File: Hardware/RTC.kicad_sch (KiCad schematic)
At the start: 15 parts, among them IC1 RTC_DS3231M, U8 PCF8563TS, Y2 32.768kHz

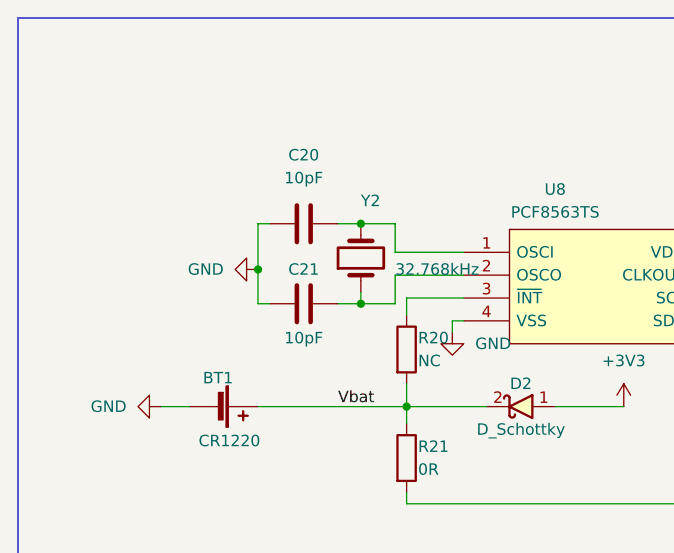
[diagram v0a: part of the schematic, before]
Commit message: Change footprint of MCP41010 and 32.768 crystal
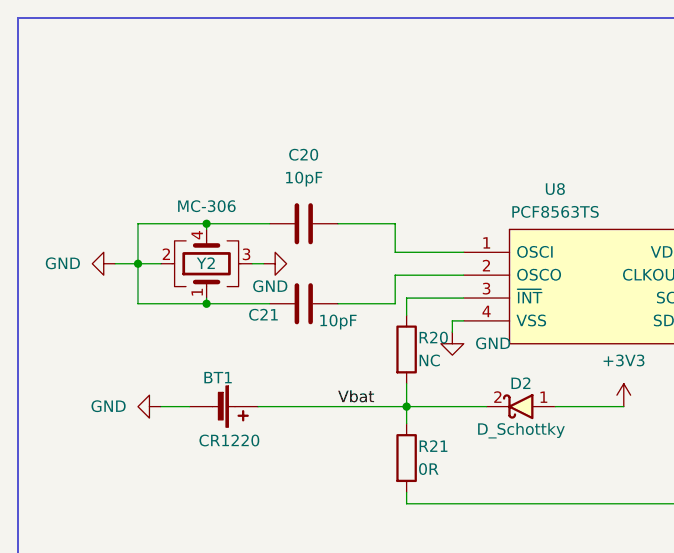
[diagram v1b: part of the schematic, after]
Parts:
- removed Y2: 32.768kHz, Crystal:Crystal_SMD_SeikoEpson_MC306-4Pin_8.0x3.2mm, symbol Device:Crystal
- added Y2: MC-306, Crystal:Crystal_SMD_SeikoEpson_MC306-4Pin_8.0x3.2mm, symbol Device:Crystal_GND23
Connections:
- net GND: now also Y2.1, Y2.2, Y2.3, Y2.4
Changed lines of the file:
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@@
 (kicad_sch (version 20211123) (generator eeschema)
   (paper "A4")
-  (junction (at 63.5 52.07) (diameter 0) (color 0 0 0 0)
-  )
-  (junction (at 74.93 55.88) (diameter 0) (color 0 0 0 0)
+  (junction (at 50.165 51.435) (diameter 0) (color 0 0 0 0)
   )
   (junction (at 118.11 50.165) (diameter 0) (color 0 0 0 0)
   )
-  (junction (at 74.93 46.99) (diameter 0) (color 0 0 0 0)
+  (junction (at 57.785 46.99) (diameter 0) (color 0 0 0 0)
   )
   (junction (at 80.01 67.31) (diameter 0) (color 0 0 0 0)
@@
   )
   (junction (at 201.93 46.99) (diameter 0) (color 0 0 0 0)
+  )
+  (junction (at 57.785 55.88) (diameter 0) (color 0 0 0 0)
   )
   (junction (at 215.9 52.07) (diameter 0) (color 0 0 0 0)
@@
     (stroke (width 0) (type default) (color 0 0 0 0))
   )
+  (wire (pts (xy 47.625 51.435) (xy 50.165 51.435))
+    (stroke (width 0) (type default) (color 0 0 0 0))
+  )
   (wire (pts (xy 218.44 43.18) (xy 218.44 55.88))
     (stroke (width 0) (type default) (color 0 0 0 0))
@@
     (stroke (width 0) (type default) (color 0 0 0 0))
   )
+  (wire (pts (xy 50.165 51.435) (xy 52.705 51.435))
+    (stroke (width 0) (type default) (color 0 0 0 0))
+  )
   (wire (pts (xy 218.44 43.18) (xy 231.14 43.18))
     (stroke (width 0) (type default) (color 0 0 0 0))
   )
+  (wire (pts (xy 57.785 55.245) (xy 57.785 55.88))
+    (stroke (width 0) (type default) (color 0 0 0 0))
+  )
   (wire (pts (xy 205.74 43.18) (xy 201.93 43.18))
     (stroke (width 0) (type default) (color 0 0 0 0))
@@
     (stroke (width 0) (type default) (color 0 0 0 0))
   )
+  (wire (pts (xy 50.165 46.99) (xy 57.785 46.99))
+    (stroke (width 0) (type default) (color 0 0 0 0))
+  )
   (wire (pts (xy 80.01 67.31) (xy 88.9 67.31))
     (stroke (width 0) (type default) (color 0 0 0 0))
   )
-  (wire (pts (xy 74.93 54.61) (xy 74.93 55.88))
-    (stroke (width 0) (type default) (color 0 0 0 0))
-  )
   (wire (pts (xy 78.74 52.705) (xy 86.36 52.705))
     (stroke (width 0) (type default) (color 0 0 0 0))
@@
     (stroke (width 0) (type default) (color 0 0 0 0))
   )
-  (wire (pts (xy 63.5 52.07) (xy 63.5 55.88))
-    (stroke (width 0) (type default) (color 0 0 0 0))
-  )
   (wire (pts (xy 199.39 46.99) (xy 201.93 46.99))
     (stroke (width 0) (type default) (color 0 0 0 0))
@@
     (stroke (width 0) (type default) (color 0 0 0 0))
   )
-  (wire (pts (xy 64.77 55.88) (xy 63.5 55.88))
-    (stroke (width 0) (type default) (color 0 0 0 0))
-  )
   (wire (pts (xy 80.01 69.215) (xy 80.01 67.31))
     (stroke (width 0) (type default) (color 0 0 0 0))
@@
     (stroke (width 0) (type default) (color 0 0 0 0))
   )
-  (wire (pts (xy 63.5 46.99) (xy 64.77 46.99))
-    (stroke (width 0) (type default) (color 0 0 0 0))
-  )
   (wire (pts (xy 118.11 33.655) (xy 118.11 36.83))
     (stroke (width 0) (type default) (color 0 0 0 0))
@@
     (stroke (width 0) (type default) (color 0 0 0 0))
   )
+  (wire (pts (xy 57.785 55.88) (xy 64.77 55.88))
+    (stroke (width 0) (type default) (color 0 0 0 0))
+  )
   (polyline (pts (xy 170.18 104.14) (xy 264.16 104.14))
     (stroke (width 0) (type default) (color 0 0 0 0))
@@
     (stroke (width 0) (type default) (color 0 0 0 0))
   )
-  (wire (pts (xy 63.5 46.99) (xy 63.5 52.07))
+  (wire (pts (xy 50.165 46.99) (xy 50.165 51.435))
     (stroke (width 0) (type default) (color 0 0 0 0))
   )
@@
     (stroke (width 0) (type default) (color 0 0 0 0))
   )
+  (wire (pts (xy 57.785 46.99) (xy 57.785 47.625))
+    (stroke (width 0) (type default) (color 0 0 0 0))
+  )
   (polyline (pts (xy 170.18 25.4) (xy 170.18 104.14))
     (stroke (width 0) (type default) (color 0 0 0 0))
@@
     (stroke (width 0) (type default) (color 0 0 0 0))
   )
-  (wire (pts (xy 72.39 46.99) (xy 74.93 46.99))
-    (stroke (width 0) (type default) (color 0 0 0 0))
-  )
   (wire (pts (xy 78.74 52.705) (xy 78.74 55.88))
     (stroke (width 0) (type default) (color 0 0 0 0))
   )
+  (wire (pts (xy 62.865 51.435) (xy 64.135 51.435))
+    (stroke (width 0) (type default) (color 0 0 0 0))
+  )
   (wire (pts (xy 215.9 43.18) (xy 215.9 52.07))
     (stroke (width 0) (type default) (color 0 0 0 0))
@@
     (stroke (width 0) (type default) (color 0 0 0 0))
   )
+  (wire (pts (xy 50.165 51.435) (xy 50.165 55.88))
+    (stroke (width 0) (type default) (color 0 0 0 0))
+  )
   (wire (pts (xy 86.36 50.165) (xy 78.74 50.165))
     (stroke (width 0) (type default) (color 0 0 0 0))
@@
     (stroke (width 0) (type default) (color 0 0 0 0))
   )
-  (wire (pts (xy 72.39 55.88) (xy 74.93 55.88))
+  (wire (pts (xy 72.39 55.88) (xy 78.74 55.88))
     (stroke (width 0) (type default) (color 0 0 0 0))
   )
@@
     (stroke (width 0) (type default) (color 0 0 0 0))
   )
+  (wire (pts (xy 57.785 46.99) (xy 64.77 46.99))
+    (stroke (width 0) (type default) (color 0 0 0 0))
+  )
   (wire (pts (xy 80.01 78.105) (xy 118.11 78.105))
     (stroke (width 0) (type default) (color 0 0 0 0))
   )
-  (wire (pts (xy 74.93 55.88) (xy 78.74 55.88))
-    (stroke (width 0) (type default) (color 0 0 0 0))
-  )
   (wire (pts (xy 243.84 43.18) (xy 243.84 41.91))
     (stroke (width 0) (type default) (color 0 0 0 0))
   )
-  (wire (pts (xy 74.93 46.99) (xy 78.74 46.99))
+  (wire (pts (xy 72.39 46.99) (xy 78.74 46.99))
     (stroke (width 0) (type default) (color 0 0 0 0))
   )
@@
   )
   (polyline (pts (xy 264.16 24.13) (xy 170.18 24.13))
+    (stroke (width 0) (type default) (color 0 0 0 0))
+  )
+  (wire (pts (xy 50.165 55.88) (xy 57.785 55.88))
     (stroke (width 0) (type default) (color 0 0 0 0))
   )
@@
     )
     (property "Datasheet" "" (id 3) (at 231.14 45.72 0)
-      (effects (font (size 1.27 1.27)) hide)
-    )
-    (pin "1")
-    (pin "2")
-  )
-  (symbol (lib_id "Device:Crystal") (at 74.93 50.8 90) (unit 1)
-    (in_bom yes) (on_board yes)
-    (property "Reference" "Y2" (id 0) (at 74.93 44.45 90)
-      (effects (font (size 1.27 1.27)) (justify right))
-    )
-    (property "Value" "32.768kHz" (id 1) (at 78.74 52.07 90)
-      (effects (font (size 1.27 1.27)) (justify right))
-    )
-    (property "Footprint" "Crystal:Crystal_SMD_SeikoEpson_MC306-4Pin_8.0x3.2mm" (id 2) (at 74.93 50.8 0)
-      (effects (font (size 1.27 1.27)) hide)
-    )
-    (property "Datasheet" "~" (id 3) (at 74.93 50.8 0)
       (effects (font (size 1.27 1.27)) hide)
     )
@@
   (symbol (lib_id "Device:C") (at 68.58 55.88 90) (unit 1)
     (in_bom yes) (on_board yes)
-    (property "Reference" "C21" (id 0) (at 68.58 52.07 90))
-    (property "Value" "10pF" (id 1) (at 68.58 59.69 90))
+    (property "Reference" "C21" (id 0) (at 64.135 57.15 90))
+    (property "Value" "10pF" (id 1) (at 72.39 57.785 90))
     (property "Footprint" "IVS_FOOTPRINTS:C0603" (id 2) (at 72.39 54.9148 0)
       (effects (font (size 1.27 1.27)) hide)
@@
     (pin "2")
   )
-  (symbol (lib_id "power:GND") (at 63.5 52.07 270) (unit 1)
-    (in_bom yes) (on_board yes) (fields_autoplaced)
-    (property "Reference" "#PWR052" (id 0) (at 57.15 52.07 0)
-      (effects (font (size 1.27 1.27)) hide)
-    )
-    (property "Value" "GND" (id 1) (at 59.69 52.0699 90)
+  (symbol (lib_id "power:GND") (at 47.625 51.435 270) (unit 1)
+    (in_bom yes) (on_board yes) (fields_autoplaced)
+    (property "Reference" "#PWR052" (id 0) (at 41.275 51.435 0)
+      (effects (font (size 1.27 1.27)) hide)
+    )
+    (property "Value" "GND" (id 1) (at 43.815 51.4349 90)
       (effects (font (size 1.27 1.27)) (justify right))
     )
-    (property "Footprint" "" (id 2) (at 63.5 52.07 0)
-      (effects (font (size 1.27 1.27)) hide)
-    )
-    (property "Datasheet" "" (id 3) (at 63.5 52.07 0)
+    (property "Footprint" "" (id 2) (at 47.625 51.435 0)
+      (effects (font (size 1.27 1.27)) hide)
+    )
+    (property "Datasheet" "" (id 3) (at 47.625 51.435 0)
       (effects (font (size 1.27 1.27)) hide)
     )
@@
     (pin "1")
   )
+  (symbol (lib_id "power:GND") (at 64.135 51.435 90) (unit 1)
+    (in_bom yes) (on_board yes)
+    (property "Reference" "#PWR0182" (id 0) (at 70.485 51.435 0)
+      (effects (font (size 1.27 1.27)) hide)
+    )
+    (property "Value" "GND" (id 1) (at 62.865 53.975 90)
+      (effects (font (size 1.27 1.27)) (justify right))
+    )
+    (property "Footprint" "" (id 2) (at 64.135 51.435 0)
+      (effects (font (size 1.27 1.27)) hide)
+    )
+    (property "Datasheet" "" (id 3) (at 64.135 51.435 0)
+      (effects (font (size 1.27 1.27)) hide)
+    )
+    (pin "1")
+  )
   (symbol (lib_id "power:+3V3") (at 243.84 41.91 0) (unit 1)
     (in_bom yes) (on_board yes) (fields_autoplaced)
@@
     (pin "2")
   )
+  (symbol (lib_id "Device:Crystal_GND23") (at 57.785 51.435 90) (unit 1)
+    (in_bom yes) (on_board yes)
+    (property "Reference" "Y2" (id 0) (at 57.785 51.435 90))
+    (property "Value" "MC-306" (id 1) (at 57.785 45.085 90))
+    (property "Footprint" "Crystal:Crystal_SMD_SeikoEpson_MC306-4Pin_8.0x3.2mm" (id 2) (at 57.785 51.435 0)
+      (effects (font (size 1.27 1.27)) hide)
+    )
+    (property "Datasheet" "~" (id 3) (at 57.785 51.435 0)
+      (effects (font (size 1.27 1.27)) hide)
+    )
+    (pin "1")
+    (pin "2")
+    (pin "3")
+    (pin "4")
+  )
   (symbol (lib_id "power:GND") (at 52.705 67.31 270) (unit 1)

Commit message: add shematics MVA
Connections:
- net GND: now also C20.2, C21.2; no longer C20.1, C21.1, Y2.1, Y2.4
- net at U8.2 (OSCO): now also C21.1, Y2.1; no longer C21.2
- net at U8.1 (OSCI): now also C20.1, Y2.4; no longer C20.2
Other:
- moved on the sheet: C20, C21
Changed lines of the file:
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@@
 (kicad_sch (version 20230121) (generator eeschema)
   (paper "A4")
-  (junction (at 50.165 51.435) (diameter 0) (color 0 0 0 0)
+  (junction (at 70.485 52.07) (diameter 0) (color 0 0 0 0)
   )
   (junction (at 118.11 50.165) (diameter 0) (color 0 0 0 0)
@@
     (stroke (width 0) (type default))
   )
-  (wire (pts (xy 47.625 51.435) (xy 50.165 51.435))
+  (wire (pts (xy 69.215 52.07) (xy 70.485 52.07))
     (stroke (width 0) (type default))
   )
@@
     (stroke (width 0) (type default))
   )
-  (wire (pts (xy 50.165 51.435) (xy 52.705 51.435))
-    (stroke (width 0) (type default))
-  )
   (wire (pts (xy 218.44 43.18) (xy 231.14 43.18))
     (stroke (width 0) (type default))
@@
     (stroke (width 0) (type default))
   )
+  (wire (pts (xy 70.485 52.07) (xy 71.755 52.07))
+    (stroke (width 0) (type default))
+  )
   (polyline (pts (xy 170.18 24.13) (xy 170.18 25.4))
     (stroke (width 0) (type default))
@@
     (stroke (width 0) (type default))
   )
-  (wire (pts (xy 50.165 46.99) (xy 57.785 46.99))
-    (stroke (width 0) (type default))
-  )
   (wire (pts (xy 80.01 67.31) (xy 88.9 67.31))
     (stroke (width 0) (type default))
@@
     (stroke (width 0) (type default))
   )
+  (wire (pts (xy 68.58 55.88) (xy 70.485 55.88))
+    (stroke (width 0) (type default))
+  )
   (polyline (pts (xy 36.83 24.13) (xy 36.83 104.14))
     (stroke (width 0) (type default))
@@
     (stroke (width 0) (type default))
   )
+  (wire (pts (xy 69.215 51.435) (xy 62.865 51.435))
+    (stroke (width 0) (type default))
+  )
   (wire (pts (xy 199.39 46.99) (xy 201.93 46.99))
     (stroke (width 0) (type default))
@@
     (stroke (width 0) (type default))
   )
+  (wire (pts (xy 78.74 59.69) (xy 57.785 59.69))
+    (stroke (width 0) (type default))
+  )
   (wire (pts (xy 118.11 33.655) (xy 118.11 36.83))
     (stroke (width 0) (type default))
   )
+  (wire (pts (xy 70.485 46.99) (xy 70.485 52.07))
+    (stroke (width 0) (type default))
+  )
   (bus (pts (xy 134.62 64.77) (xy 137.16 64.77))
     (stroke (width 0) (type default))
@@
     (stroke (width 0) (type default))
   )
-  (wire (pts (xy 57.785 55.88) (xy 64.77 55.88))
+  (wire (pts (xy 57.785 55.88) (xy 60.96 55.88))
     (stroke (width 0) (type default))
   )
@@
     (stroke (width 0) (type default))
   )
-  (wire (pts (xy 78.74 46.99) (xy 78.74 50.165))
-    (stroke (width 0) (type default))
-  )
-  (wire (pts (xy 50.165 46.99) (xy 50.165 51.435))
+  (wire (pts (xy 78.74 43.18) (xy 78.74 50.165))
+    (stroke (width 0) (type default))
+  )
+  (wire (pts (xy 68.58 46.99) (xy 70.485 46.99))
     (stroke (width 0) (type default))
   )
@@
     (stroke (width 0) (type default))
   )
-  (wire (pts (xy 78.74 52.705) (xy 78.74 55.88))
-    (stroke (width 0) (type default))
-  )
-  (wire (pts (xy 62.865 51.435) (xy 64.135 51.435))
+  (wire (pts (xy 78.74 52.705) (xy 78.74 59.69))
+    (stroke (width 0) (type default))
+  )
+  (wire (pts (xy 57.785 46.99) (xy 60.96 46.99))
     (stroke (width 0) (type default))
   )
@@
     (stroke (width 0) (type default))
   )
-  (wire (pts (xy 50.165 51.435) (xy 50.165 55.88))
+  (wire (pts (xy 78.74 43.18) (xy 57.785 43.18))
     (stroke (width 0) (type default))
   )
@@
     (stroke (width 0) (type default))
   )
+  (wire (pts (xy 70.485 52.07) (xy 70.485 55.88))
+    (stroke (width 0) (type default))
+  )
   (wire (pts (xy 215.9 41.91) (xy 215.9 43.18))
     (stroke (width 0) (type default))
@@
     (stroke (width 0) (type default))
   )
+  (wire (pts (xy 69.215 52.07) (xy 69.215 51.435))
+    (stroke (width 0) (type default))
+  )
   (wire (pts (xy 201.93 43.18) (xy 201.93 46.99))
     (stroke (width 0) (type default))
   )
-  (wire (pts (xy 72.39 55.88) (xy 78.74 55.88))
+  (wire (pts (xy 57.785 43.18) (xy 57.785 46.99))
     (stroke (width 0) (type default))
   )
@@
     (stroke (width 0) (type default))
   )
-  (wire (pts (xy 57.785 46.99) (xy 64.77 46.99))
+  (wire (pts (xy 57.785 59.69) (xy 57.785 55.88))
     (stroke (width 0) (type default))
   )
@@
     (stroke (width 0) (type default))
   )
-  (wire (pts (xy 72.39 46.99) (xy 78.74 46.99))
-    (stroke (width 0) (type default))
-  )
   (wire (pts (xy 85.09 59.055) (xy 85.09 57.785))
     (stroke (width 0) (type default))
   )
   (polyline (pts (xy 264.16 24.13) (xy 170.18 24.13))
-    (stroke (width 0) (type default))
-  )
-  (wire (pts (xy 50.165 55.88) (xy 57.785 55.88))
     (stroke (width 0) (type default))
   )
@@
     )
   )
-  (symbol (lib_id "Device:C") (at 68.58 55.88 90) (unit 1)
+  (symbol (lib_id "Device:C") (at 64.77 55.88 90) (unit 1)
     (in_bom yes) (on_board yes) (dnp no)
-    (property "Reference" "C21" (at 64.135 57.15 90)
-      (effects (font (size 1.27 1.27)))
-    )
-    (property "Value" "10pF" (at 72.39 57.785 90)
-      (effects (font (size 1.27 1.27)))
-    )
-    (property "Footprint" "IVS_FOOTPRINTS:C0603" (at 72.39 54.9148 0)
-      (effects (font (size 1.27 1.27)) hide)
-    )
-    (property "Datasheet" "~" (at 68.58 55.88 0)
+    (property "Reference" "C21" (at 60.325 57.15 90)
+      (effects (font (size 1.27 1.27)))
+    )
+    (property "Value" "10pF" (at 68.58 57.785 90)
+      (effects (font (size 1.27 1.27)))
+    )
+    (property "Footprint" "IVS_FOOTPRINTS:C0603" (at 68.58 54.9148 0)
+      (effects (font (size 1.27 1.27)) hide)
+    )
+    (property "Datasheet" "~" (at 64.77 55.88 0)
       (effects (font (size 1.27 1.27)) hide)
     )
@@
     )
   )
-  (symbol (lib_id "power:GND") (at 47.625 51.435 270) (unit 1)
-    (in_bom yes) (on_board yes) (dnp no) (fields_autoplaced)
-    (property "Reference" "#PWR052" (at 41.275 51.435 0)
-      (effects (font (size 1.27 1.27)) hide)
-    )
-    (property "Value" "GND" (at 43.815 51.4349 90)
+  (symbol (lib_id "power:GND") (at 52.705 51.435 270) (unit 1)
+    (in_bom yes) (on_board yes) (dnp no) (fields_autoplaced)
+    (property "Reference" "#PWR052" (at 46.355 51.435 0)
+      (effects (font (size 1.27 1.27)) hide)
+    )
+    (property "Value" "GND" (at 48.895 51.4349 90)
       (effects (font (size 1.27 1.27)) (justify right))
     )
-    (property "Footprint" "" (at 47.625 51.435 0)
-      (effects (font (size 1.27 1.27)) hide)
-    )
-    (property "Datasheet" "" (at 47.625 51.435 0)
+    (property "Footprint" "" (at 52.705 51.435 0)
+      (effects (font (size 1.27 1.27)) hide)
+    )
+    (property "Datasheet" "" (at 52.705 51.435 0)
       (effects (font (size 1.27 1.27)) hide)
     )
@@
     )
   )
-  (symbol (lib_id "power:GND") (at 64.135 51.435 90) (unit 1)
+  (symbol (lib_id "power:GND") (at 71.755 52.07 90) (unit 1)
     (in_bom yes) (on_board yes) (dnp no)
-    (property "Reference" "#PWR0182" (at 70.485 51.435 0)
-      (effects (font (size 1.27 1.27)) hide)
-    )
-    (property "Value" "GND" (at 62.865 53.975 90)
+    (property "Reference" "#PWR0182" (at 78.105 52.07 0)
+      (effects (font (size 1.27 1.27)) hide)
+    )
+    (property "Value" "GND" (at 70.485 54.61 90)
       (effects (font (size 1.27 1.27)) (justify right))
     )
-    (property "Footprint" "" (at 64.135 51.435 0)
-      (effects (font (size 1.27 1.27)) hide)
-    )
-    (property "Datasheet" "" (at 64.135 51.435 0)
+    (property "Footprint" "" (at 71.755 52.07 0)
+      (effects (font (size 1.27 1.27)) hide)
+    )
+    (property "Datasheet" "" (at 71.755 52.07 0)
       (effects (font (size 1.27 1.27)) hide)
     )
@@
     )
   )
-  (symbol (lib_id "Device:C") (at 68.58 46.99 90) (unit 1)
-    (in_bom yes) (on_board yes) (dnp no) (fields_autoplaced)
-    (property "Reference" "C20" (at 68.58 39.37 90)
-      (effects (font (size 1.27 1.27)))
-    )
-    (property "Value" "10pF" (at 68.58 41.91 90)
-      (effects (font (size 1.27 1.27)))
-    )
-    (property "Footprint" "IVS_FOOTPRINTS:C0603" (at 72.39 46.0248 0)
-      (effects (font (size 1.27 1.27)) hide)
-    )
-    (property "Datasheet" "~" (at 68.58 46.99 0)
-      (effects (font (size 1.27 1.27)) hide)
-    )
+  (symbol (lib_id "Device:C") (at 64.77 46.99 90) (unit 1)
+    (in_bom yes) (on_board yes) (dnp no) (fields_autoplaced)
+    (property "Reference" "C20" (at 64.77 39.37 90)
+      (effects (font (size 1.27 1.27)))
+    )
+    (property "Value" "10pF" (at 64.77 41.91 90)
+      (effects (font (size 1.27 1.27)))
+    )
+    (property "Footprint" "IVS_FOOTPRINTS:C0603" (at 68.58 46.0248 0)
+      (effects (font (size 1.27 1.27)) hide)
+    )
+    (property "Datasheet" "~" (at 64.77 46.99 0)
+      (effects (font (size 1.27 1.27)) hide)
+    )

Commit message: layout PCB part 1
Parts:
- removed D2, D3, D4: D_Schottky, IVS_FOOTPRINTS:D_SMA, symbol IVS_SYMBOL_DIR:D_Schottky
- added D1, D2: BAT54C, IVS_FOOTPRINTS:SOT23-3, symbol IVS_SYMBOLS:BAT54C
- added R42: 1k, IVS_FOOTPRINTS:R0603, symbol Device:R
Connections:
- net +3V3: now also D2.3, R42.1
- net Vbat: now also D1.2, D2.2
- net at IC1.14 (VBAT): now also D1.3
- new net: D1.1, R42.2
- no-connect marks 1 -> 5
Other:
- moved on the sheet: BT1, R21, R22

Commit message: layout part 2
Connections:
- net Vbat: now also D2.1; no longer D2.2
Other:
- moved on the sheet: D2
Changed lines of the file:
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@@
+    (stroke (width 0) (type default))
+  )
+  (wire (pts (xy 80.01 73.66) (xy 88.9 73.66))
     (stroke (width 0) (type default))
   )
@@
   )
   (wire (pts (xy 80.01 84.455) (xy 118.11 84.455))
-    (stroke (width 0) (type default))
-  )
-  (wire (pts (xy 80.01 73.66) (xy 88.9 73.66))
     (stroke (width 0) (type default))
   )
@@
     )
   )
-  (symbol (lib_id "IVS_SYMBOLS:BAT54C") (at 96.52 73.66 180) (unit 1)
+  (symbol (lib_id "IVS_SYMBOLS:BAT54C") (at 96.52 73.66 0) (mirror x) (unit 1)
     (in_bom yes) (on_board yes) (dnp no)
     (property "Reference" "D2" (at 96.52 76.835 0)
@@
       (effects (font (size 1.27 1.27)))
     )
-    (property "Footprint" "IVS_FOOTPRINTS:SOT23-3" (at 109.22 60.96 0)
-      (effects (font (size 1.27 1.27)) (justify left) hide)
-    )
+    (property "Footprint" "IVS_FOOTPRINTS:SOT23-3" (at 83.82 60.96 0)
+      (effects (font (size 1.27 1.27)) (justify left) hide)
+    )
